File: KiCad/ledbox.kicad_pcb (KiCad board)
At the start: 2 copper layers, 80 x 50 mm, 102 parts, among them CON301 AVR_ISP, J201 Bus, J301 Power B, J302 Port B, J303 Spare, J304 UART, J305 ADC6, J306 ADC7, J401 6.5V-12V, J402 5V, J501 IR LED, J502 Button, Q501 NTR4003N, SW501 Reset, SW502 Push 1, SW503 Push 2, U201 ST485C, U301 ATMEGA88A-AU, U401 AZ1117-5.0, U501 WS2812B, U502 WS2812B, U503 3xWS2812B, Y301 20MHz

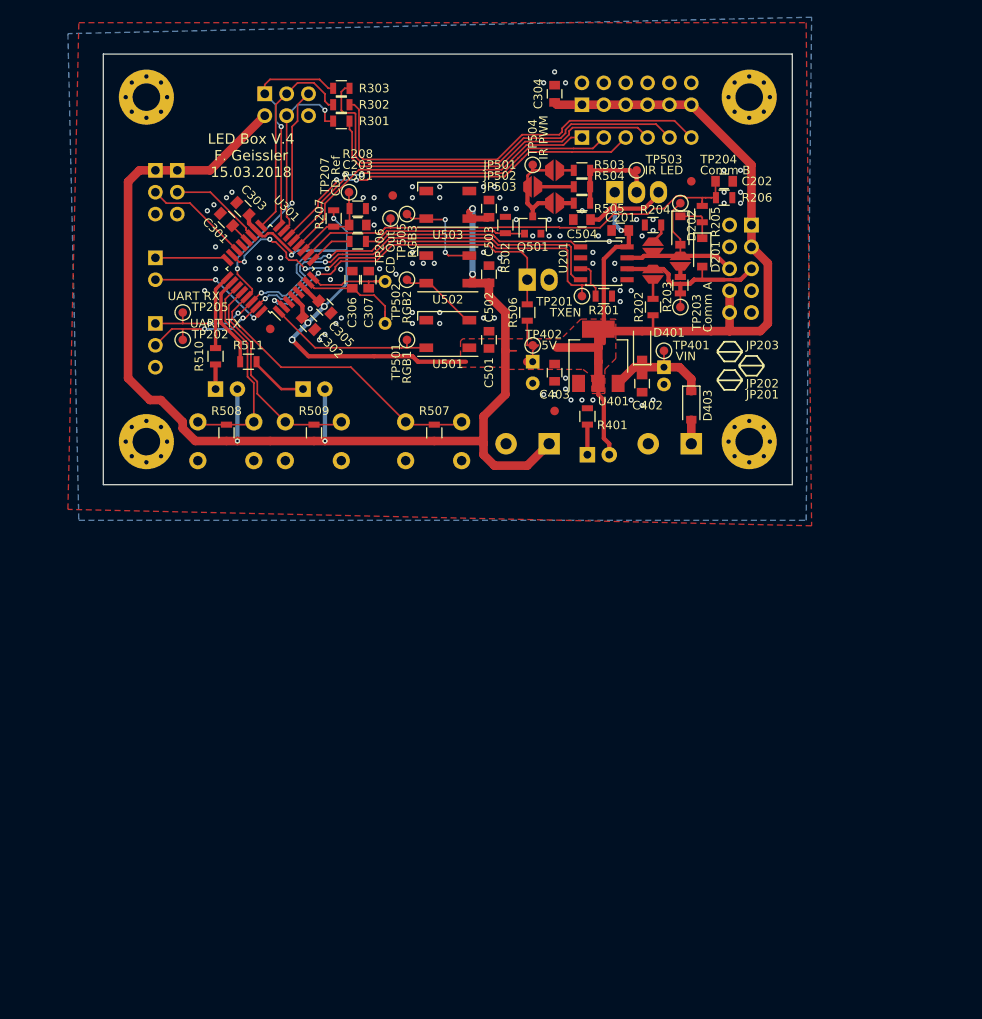
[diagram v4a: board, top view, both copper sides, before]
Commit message: Version 4 Shift Register
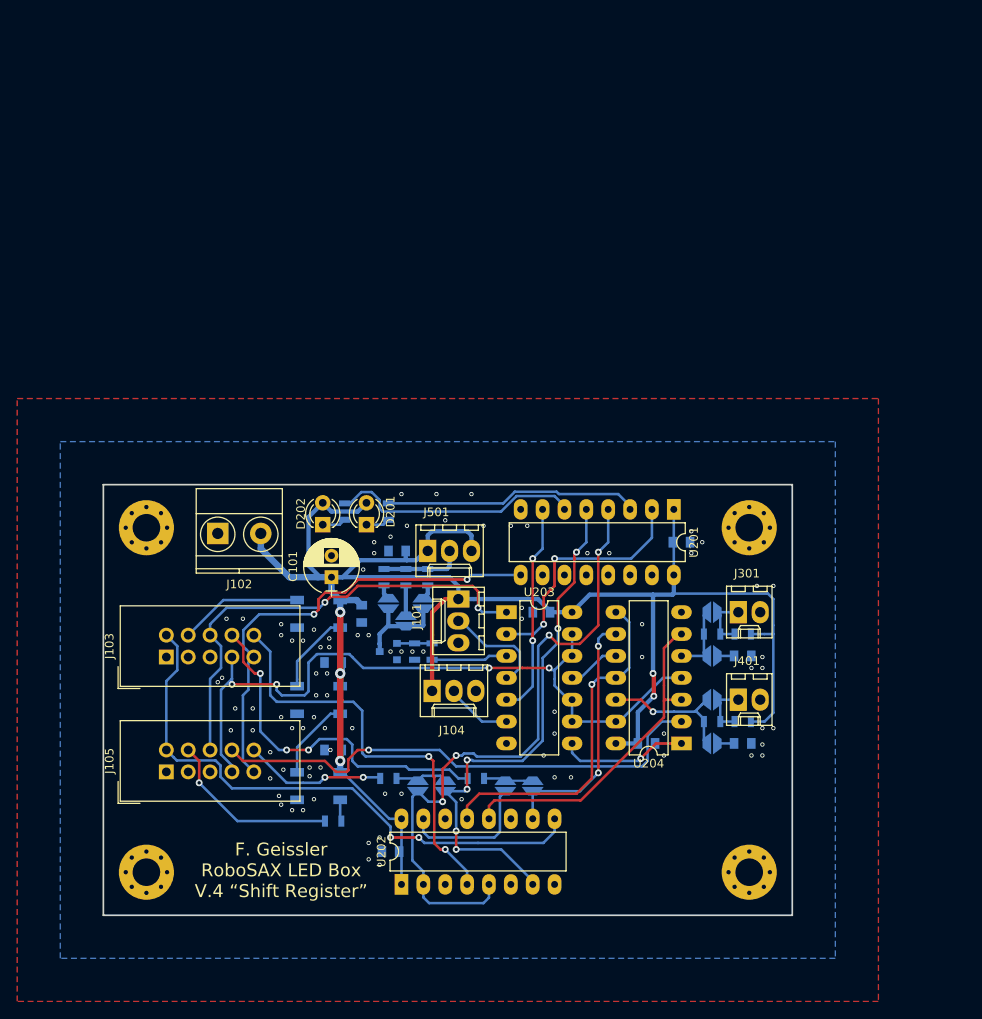
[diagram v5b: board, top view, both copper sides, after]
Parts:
- removed C302, C303, C304, C305, C402, C403: 100n, Capacitors_SMD:C_0805
- removed C306, C307: 22p, Capacitors_SMD:C_0805
- removed C404: 47u, Capacitors_THT:CP_Radial_D6.3mm_P2.50mm
- removed CON301: AVR_ISP, Connectors_IDC:IDC-Header_2x03_Pitch2.54mm_Straight
- removed D401: 1N4148, Diodes_SMD:D_SOD-123
- removed D402, D502: LED2, LEDs:LED_D3.0mm
- removed D403: PMEG4010ER, Diodes_SMD:D_SOD-123
- removed D501: LED1, LEDs:LED_D3.0mm
- removed the G*** at (139.0, 89.0)
- removed the G*** at (140.0, 75.0)
- removed the G*** at (140.0, 56.0)
- removed J201: Bus, Connectors_IDC:IDC-Header_2x05_Pitch2.54mm_Straight
- removed J302: Port B, Socket_Strips:Socket_Strip_Straight_1x06_Pitch2.54mm
- removed J303: Spare, Socket_Strips:Socket_Strip_Straight_1x02_Pitch2.54mm
- removed J304: UART, Socket_Strips:Socket_Strip_Straight_1x03_Pitch2.54mm
- removed J305: ADC6, Socket_Strips:Socket_Strip_Straight_1x03_Pitch2.54mm
- removed J306: ADC7, Socket_Strips:Socket_Strip_Straight_1x03_Pitch2.54mm
- removed J402: 5V, TerminalBlock_MetzConnect:TerminalBlock_MetzConnect_Type055_RT01502HDWU_Pitch5.00mm
- removed J502: Button, Connectors_Molex:Molex_KK-6410-02_02x2.54mm_Straight
- removed R203: 150, Resistors_SMD:R_0805
- removed R204, R303: 1k, Resistors_SMD:R_0805
- removed R205: 100, Resistors_SMD:R_0805
- removed R206: 22k, Resistors_SMD:R_0805
- removed R207: 3k3, Resistors_SMD:R_0805
- removed R208: 2k2, Resistors_SMD:R_0805
- removed R506, R507, R508, R509: 10k, Resistors_SMD:R_0805
- removed R510, R511: 430, Resistors_SMD:R_0805
- removed the REF** at (133.6, 66.4)
- removed the REF** at (168.3, 64.8)
- removed the REF** at (152.4, 91.4)
- removed the REF** at (119.4, 81.9)
- removed the REF** at (105.0, 95.0)
- removed the REF** at (105.0, 55.0)
- removed the REF** at (175.0, 55.0)
- removed the REF** at (175.0, 95.0)
- removed SW501: Reset, Buttons_Switches_THT:SW_PUSH_6mm_h5mm
- removed SW502: Push 1, Buttons_Switches_THT:SW_PUSH_6mm_h5mm
- removed SW503: Push 2, Buttons_Switches_THT:SW_PUSH_6mm_h5mm
- removed TP201: TXEN, Test:TEST_10
- removed TP202: UART TX, Test:TEST_10
- removed TP203: Comm A, Test:TEST_10
- removed TP204: Comm B, Test:TEST_10
- removed TP205: UART RX, Test:TEST_10
- removed TP206: CD Out, Test:TEST_10
- removed TP207: CD Ref, Test:TEST_10
- removed TP401: VIN, Test:TEST_10
- removed TP402: 5V, Test:TEST_10
- removed TP501: RGB1, Test:TEST_10
- removed TP502: RGB2, Test:TEST_10
- removed TP503: IR LED, Test:TEST_10
- removed TP504: IR PWM, Test:TEST_10
- removed TP505: RGB3, Test:TEST_10
- removed U301: ATMEGA88A-AU, Housings_QFP:TQFP-32_7x7mm_Pitch0.8mm
- removed U401: AZ1117-5.0, TO_SOT_Packages_SMD:SOT-223-3_TabPin2
- removed Y301: 20MHz, Crystals:Crystal_HC49-U_Vertical
- added C101: 10u, Capacitors_THT:CP_Radial_D6.3mm_P2.50mm, F.Cu at (126.5, 110.7)
- added C204: 100n, Capacitors_SMD:C_0805, B.Cu at (133.3, 142.6)
- added G***: LOGO, LOGO, F.Cu at (162.1, 141.7)
- added J101: Add Input, Connectors_Molex:Molex_KK-6410-03_03x2.54mm_Straight, F.Cu at (141.2, 113.3)
- added J102: 5V, TerminalBlock_Phoenix:TerminalBlock_Phoenix_MKDS1.5-2pol, F.Cu at (113.3, 105.7)
- added J103: To Master, Connectors_IDC:IDC-Header_2x05_Pitch2.54mm_Straight, F.Cu at (107.3, 120.0)
- added J104: Add Output, Connectors_Molex:Molex_KK-6410-03_03x2.54mm_Straight, F.Cu at (138.2, 124.0)
- added J105: To Slave, Connectors_IDC:IDC-Header_2x05_Pitch2.54mm_Straight, F.Cu at (107.3, 133.3)
- added JP204: Add In, SMD_Jumper:Jumper_SMD_02, B.Cu at (146.7, 135.0)
- added JP301: ~Debounce, SMD_Jumper:Jumper_SMD_02, B.Cu at (170.7, 114.8)
- added JP302: Debounce, SMD_Jumper:Jumper_SMD_02, B.Cu at (170.7, 119.9)
- added JP401: ~Debounce, SMD_Jumper:Jumper_SMD_02, B.Cu at (170.7, 125.0)
- added JP402: Debounce, SMD_Jumper:Jumper_SMD_02, B.Cu at (170.7, 130.0)
- added R101: 120, Resistors_SMD:R_0805, B.Cu at (143.3, 134.1)
- added R102: 120, Resistors_SMD:R_0805, B.Cu at (133.1, 134.1)
- added R103: 120, Resistors_SMD:R_0805, B.Cu at (126.7, 139.1)
- added R402: 47k, Resistors_SMD:R_0805, B.Cu at (170.7, 127.5)
- added REF**: MountingHole_3.2mm_M3_Pad_Via, Mounting_Holes:MountingHole_3.2mm_M3_Pad_Via, F.Cu at (105.0, 105.0)
- added REF**: MountingHole_3.2mm_M3_Pad_Via, Mounting_Holes:MountingHole_3.2mm_M3_Pad_Via, F.Cu at (105.0, 145.0)
- added REF**: MountingHole_3.2mm_M3_Pad_Via, Mounting_Holes:MountingHole_3.2mm_M3_Pad_Via, F.Cu at (175.0, 145.0)
- added REF**: MountingHole_3.2mm_M3_Pad_Via, Mounting_Holes:MountingHole_3.2mm_M3_Pad_Via, F.Cu at (175.0, 105.0)
- added U202: 74LS175, Housings_DIP:DIP-16_W7.62mm_LongPads, F.Cu at (134.6, 146.4)
- added U203: 74LS00, Housings_DIP:DIP-14_W7.62mm_LongPads, F.Cu at (146.8, 114.8)
- added U204: 74LS126, Housings_DIP:DIP-14_W7.62mm_LongPads, F.Cu at (167.1, 130.0)
- C201: value 10u -> 100n; moved to B.Cu
- C202: value 22p -> 100n; moved to B.Cu
- C203: value 470p -> 100n; moved to B.Cu
- C301, C501, C502, C503, C504, JP501, Q501, R202, R501, U501, U502: moved to B.Cu
- C401: value 4u7 -> 100n; footprint Capacitors_THT:CP_Radial_D5.0mm_P2.00mm -> Capacitors_SMD:C_0805
- D201, D202: value 1N4148 -> LED; footprint Diodes_SMD:D_SOD-123 -> LEDs:LED_D3.0mm
- J301: value Power B -> Button; footprint Socket_Strips:Socket_Strip_Straight_2x06_Pitch2.54mm -> Connectors_Molex:Molex_KK-6410-02_02x2.54mm_Straight; moved to F.Cu
- J401: value 6.5V-12V -> Button; footprint TerminalBlock_MetzConnect:TerminalBlock_MetzConnect_Type055_RT01502HDWU_Pitch5.00mm -> Connectors_Molex:Molex_KK-6410-02_02x2.54mm_Straight; moved to F.Cu
- J501: moved to F.Cu
- JP201: value COMMA PU -> Single Out; moved to B.Cu
- JP202: value TERM -> Add Out; moved to B.Cu
- JP203: value COMMB PD -> Single In; moved to B.Cu
- JP502: value IR 24mA -> IR 36mA; moved to B.Cu
- JP503: value IR 48mA -> IR 76mA; moved to B.Cu
- R201: value 10k -> 1k; moved to B.Cu
- R301: value 1k -> 4k7; moved to B.Cu
- R302: value 1k -> 47k; moved to B.Cu
- R401: value 2k2 -> 4k7; moved to B.Cu
- R502: value 100k -> 47k; moved to B.Cu
- R503: value 300 -> 220; moved to B.Cu
- R504: value 150 -> 100; moved to B.Cu
- R505: value 75 -> 47; moved to B.Cu
- U201: value ST485C -> 74LS175; footprint Housings_SOIC:SOIC-8_3.9x4.9mm_Pitch1.27mm -> Housings_DIP:DIP-16_W7.62mm_LongPads
- U503: value 3xWS2812B -> WS2812B; moved to B.Cu
- moved C301 78.5 mm to (174.2, 119.9), turned to 0 degrees
- moved R301 75.6 mm to (174.2, 117.3)
- moved R302 75.0 mm to (170.7, 117.3), turned to 0 degrees
- moved U503 69.1 mm to (125.0, 135.0)
- moved C203 68.9 mm to (163.1, 130.0)
- moved JP202 66.8 mm to (139.7, 135.0)
- moved JP201 65.4 mm to (136.5, 135.0)
- moved JP203 64.1 mm to (149.9, 135.0)
- moved J301 61.7 mm to (173.7, 114.8), turned to 0 degrees
- moved C502 58.1 mm to (126.7, 130.8), turned to 180 degrees
- moved C503 55.7 mm to (126.7, 120.7), turned to 180 degrees
- moved C202 54.3 mm to (150.9, 114.8), turned to 180 degrees
- moved D202 53.8 mm to (125.5, 104.6), turned to 90 degrees
- moved JP501 52.6 mm to (137.2, 113.8), turned to 90 degrees
- moved JP502 52.5 mm to (135.1, 115.8), turned to 90 degrees
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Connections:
- C202 pad 1: /Bus/AIN0 -> +5V
- C203 pad 1: /Bus/AIN1 -> +5V
- C301 pad 1: GND -> Net-(C301-Pad1)
- C301 pad 2: Net-(C301-Pad2) -> GND
- C401 pad 1: +12V -> Net-(C401-Pad1)
- D201 pad 2: /Bus/COMM_A -> +5V
- D202 pad 1: Net-(D201-Pad1) -> Net-(D202-Pad1)
- D202 pad 2: /Bus/COMM_B -> +5V
- J301 pad 1: +5V -> Net-(J301-Pad1)
- J401 pad 1: Net-(D403-Pad2) -> Net-(J401-Pad1)
- JP201 pad 1: Net-(JP201-Pad1) -> /Logic/LED_OUT
- JP201 pad 2: /Bus/COMM_A -> /Logic/LED_DATA_OUT
- JP202 pad 1: Net-(JP202-Pad1) -> /Logic/LED_OUT_ADD
- JP202 pad 2: /Bus/COMM_B -> /Logic/LED_DATA_OUT
- JP203 pad 1: /Bus/COMM_B -> /Logic/BTN_OUT
- JP203 pad 2: Net-(JP203-Pad2) -> /Logic/BTN_DATA_OUT
- R201 pad 1: GND -> /Logic/LED_INDICATOR
- R201 pad 2: /Bus/TX_EN -> Net-(D201-Pad1)
- R202 pad 1: +5V -> /Logic/LED_INDICATOR_ADD
- R202 pad 2: Net-(JP201-Pad1) -> Net-(D202-Pad1)
- R301 pad 1: /Controller/PB3 -> +5V
- R301 pad 2: /Controller/MOSI -> Net-(J301-Pad1)
- R302 pad 1: /Controller/PB5 -> Net-(JP301-Pad2)
- R302 pad 2: /Controller/SCK -> Net-(J301-Pad1)
- R401 pad 1: Net-(D402-Pad1) -> +5V
- R401 pad 2: GND -> Net-(J401-Pad1)
- R501 pad 2: /Controller/LED_IR -> /Logic/IR_LED
- U201 pad 1: /Bus/RX -> +5V
- U201 pad 2: GND -> Net-(TP203-Pad1)
- U201 pad 3: /Bus/TX_EN -> /Logic/LED_INDICATOR
- U201 pad 4: /Bus/TX -> /Logic/LED_OUT
- U201 pad 5: GND -> /Logic/LED_OUT_ADD
- U201 pad 6: /Bus/COMM_A -> /Logic/LED_INDICATOR_ADD
- U201 pad 7: /Bus/COMM_B -> Net-(TP205-Pad1)
- U201 pad 8: +5V -> GND
- U501 pad 4: /Controller/RGB_D -> /RGB_IN
- U503 pad 2: Net-(U503-Pad2) -> /Interface/RGB_OUT
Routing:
- net +5V: track 338.5 -> 216.4 mm, vias 10 -> 5
- net /BTN_LOAD: track 0.00 -> 86.0 mm, vias 0 -> 4
- net /Logic/LED_OUT: track 0.00 -> 76.4 mm, vias 0 -> 4
- net /CLK: track 0.00 -> 67.5 mm, vias 0 -> 2
- net /Logic/LED_OUT_ADD: track 0.00 -> 63.2 mm, vias 0 -> 6
- net /Controller/~RESET: track 63.1 -> 0.00 mm, vias 2 -> 0
- net /Bus/TX: track 61.9 -> 0.00 mm, vias 4 -> 0
- net /BTN_DATA_IN: track 0.00 -> 59.7 mm, vias 0 -> 1
- net /Bus/RX: track 57.8 -> 0.00 mm, vias 4 -> 0
- net /Bus/TX_EN: track 57.4 -> 0.00 mm, vias 4 -> 0
- net /Bus/AIN0: track 54.8 -> 0.00 mm
- net /IR_CLK: track 0.00 -> 54.3 mm, vias 0 -> 2
- net /LED_LOAD: track 0.00 -> 53.6 mm, vias 0 -> 2
- net /Controller/PB4: track 49.5 -> 0.00 mm
- net /LED_DATA_IN: track 0.00 -> 49.0 mm, vias 0 -> 2
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- removed copper zone on F.Cu, net +5V
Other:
- net class Default: trace_width 0.2 -> 0.25; via_dia 0.6 -> 0.8; via_drill 0.3 -> 0.4
- board text added: "F. Geissler RoboSAX LED Box V.4 “Shift Register”"
- board text removed: "+"
- board text removed: "-"
- board text removed: "5V"
- board text removed: "LED Box V.4 F. Geissler 15.03.2018"

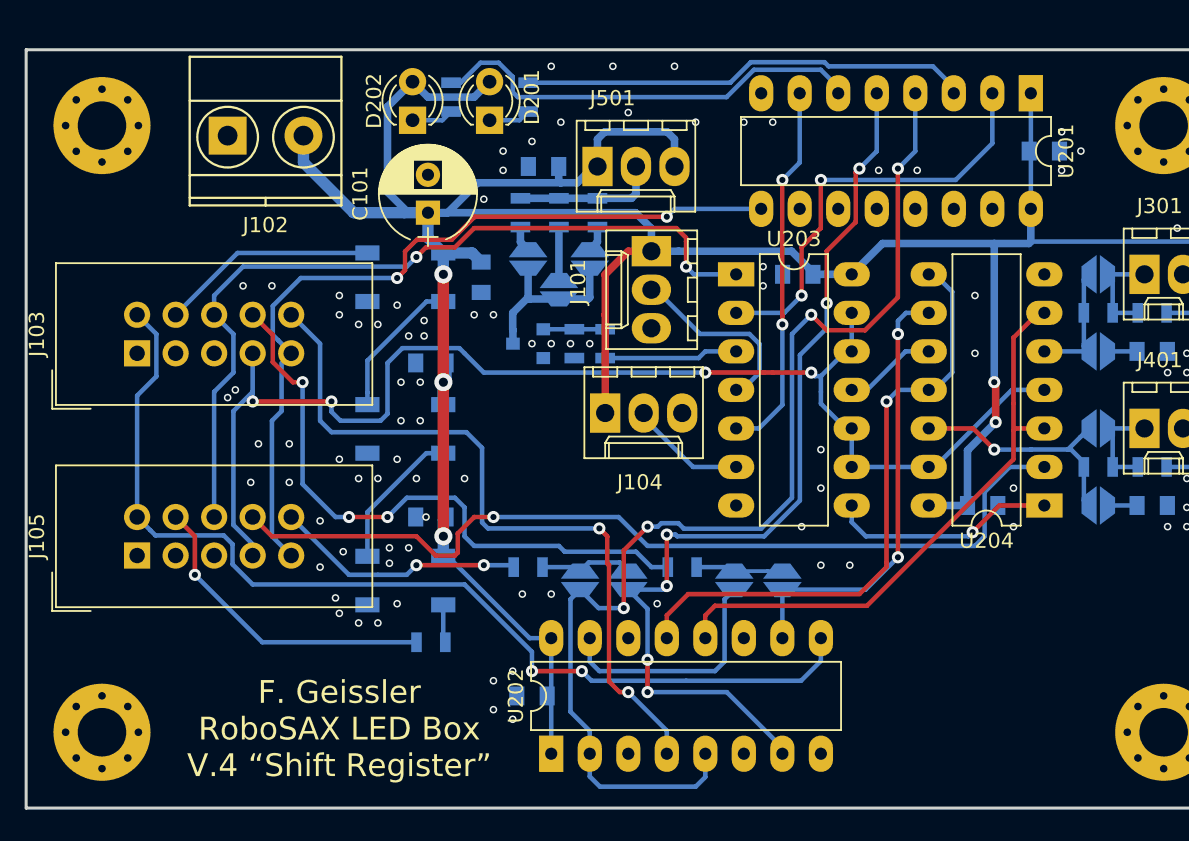
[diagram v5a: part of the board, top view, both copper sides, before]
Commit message: Applied changes for final design, placed test points.
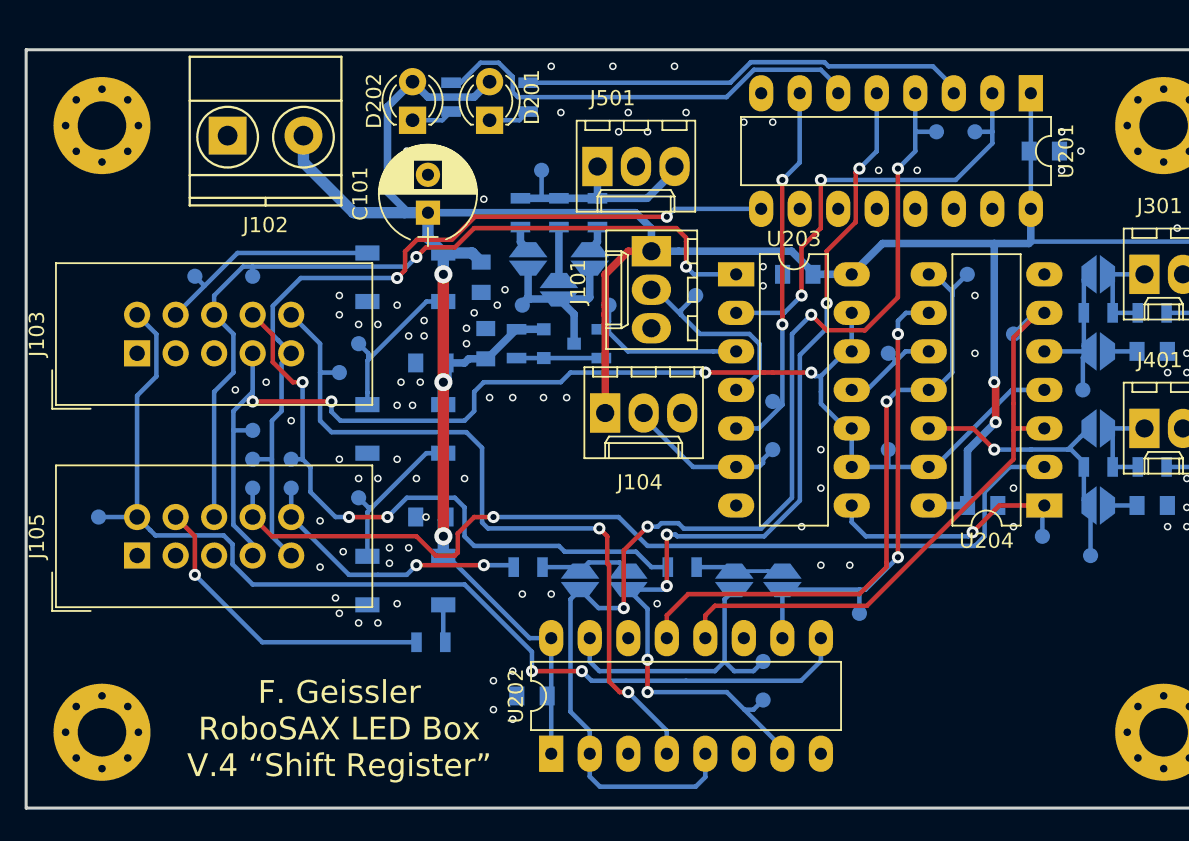
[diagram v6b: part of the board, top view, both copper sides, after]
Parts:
- added TP101: Test_Point, TestPoint:TestPoint_Pad_D1.0mm, B.Cu at (104.8, 130.8)
- added TP102: Test_Point, TestPoint:TestPoint_Pad_D1.0mm, B.Cu at (114.9, 127.0)
- added TP103: Test_Point, TestPoint:TestPoint_Pad_D1.0mm, B.Cu at (114.9, 128.9)
- added TP104: Test_Point, TestPoint:TestPoint_Pad_D1.0mm, B.Cu at (117.5, 127.0)
- added TP105: Test_Point, TestPoint:TestPoint_Pad_D1.0mm, B.Cu at (117.5, 128.9)
- added TP201: LED IN, TestPoint:TestPoint_Pad_D1.0mm, B.Cu at (120.7, 121.3)
- added TP202: Test_Point, TestPoint:TestPoint_Pad_D1.0mm, B.Cu at (114.9, 114.9)
- added TP203: Test_Point, TestPoint:TestPoint_Pad_D1.0mm, B.Cu at (162.6, 105.4)
- added TP204: Test_Point, TestPoint:TestPoint_Pad_D1.0mm, B.Cu at (144.1, 116.2)
- added TP205: Test_Point, TestPoint:TestPoint_Pad_D1.0mm, B.Cu at (149.2, 123.2)
- added TP206: Test_Point, TestPoint:TestPoint_Pad_D1.0mm, B.Cu at (138.4, 116.8)
- added TP207: Test_Point, TestPoint:TestPoint_Pad_D1.0mm, B.Cu at (149.2, 126.4)
- added TP208: LED OUT, TestPoint:TestPoint_Pad_D1.0mm, B.Cu at (160.0, 105.4)
- added TP209: ADD BTN, TestPoint:TestPoint_Pad_D1.0mm, B.Cu at (148.6, 140.3)
- added TP210: ADD OUT, TestPoint:TestPoint_Pad_D1.0mm, B.Cu at (148.6, 142.9)
- added TP211: BTN OUT, TestPoint:TestPoint_Pad_D1.0mm, B.Cu at (154.9, 137.2)
- added TP301: BTN ANA, TestPoint:TestPoint_Pad_D1.0mm, B.Cu at (169.7, 122.4)
- added TP302: BTN LOAD, TestPoint:TestPoint_Pad_D1.0mm, B.Cu at (114.9, 125.1)
- added TP303: ~BTN LOAD, TestPoint:TestPoint_Pad_D1.0mm, B.Cu at (167.0, 132.1)
- added TP304: BTN IN, TestPoint:TestPoint_Pad_D1.0mm, B.Cu at (165.1, 118.7)
- added TP401: BTN ANA, TestPoint:TestPoint_Pad_D1.0mm, B.Cu at (170.2, 133.3)
- added TP402: BTN LOAD, TestPoint:TestPoint_Pad_D1.0mm, B.Cu at (156.8, 126.4)
- added TP403: ~BTN LOAD, TestPoint:TestPoint_Pad_D1.0mm, B.Cu at (156.8, 120.0)
- added TP404: BTN IN, TestPoint:TestPoint_Pad_D1.0mm, B.Cu at (162.1, 114.8)
- added TP501: RGB1, TestPoint:TestPoint_Pad_D1.0mm, B.Cu at (111.1, 114.9)
- added TP502: RGB2, TestPoint:TestPoint_Pad_D1.0mm, B.Cu at (121.9, 119.4)
- added TP503: IR LED, TestPoint:TestPoint_Pad_D1.0mm, B.Cu at (134.0, 108.0)
- added TP504: IR PWM, TestPoint:TestPoint_Pad_D1.0mm, B.Cu at (132.7, 116.8)
- added TP505: RGB3, TestPoint:TestPoint_Pad_D1.0mm, B.Cu at (121.9, 129.5)
- Q501: value NTR4003N -> Q_PMOS_GSD; footprint TO_SOT_Packages_SMD:SOT-23 -> Package_TO_SOT_SMD:SOT-23
- moved C504 12.3 mm to (130.3, 119.4), turned to 90 degrees
- moved R502 3.81 mm to (132.3, 119.4)
- moved Q501 2.03 mm to (135.1, 119.4), turned to 0 degrees
- moved R501 0.25 mm to (137.9, 119.4), turned to 90 degrees
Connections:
- J501 pad 1: +5V -> /Interface/IR_LED_DRV
- J501 pad 2: /Interface/IR_LED_DRV -> GND
- J501 pad 3: +5V -> /Interface/IR_LED_DRV
- Q501 pad 2: GND -> +5V
- R502 pad 1: GND -> Net-(Q501-Pad1)
- R502 pad 2: Net-(Q501-Pad1) -> +5V
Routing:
- net +5V: track 216.4 -> 201.1 mm
- net /Interface/IR_LED_DRV: track 9.72 -> 15.3 mm
- net Net-(JP401-Pad2): track 16.1 -> 19.5 mm
- net Net-(JP204-Pad1): track 16.0 -> 19.0 mm
- net /Logic/ADD_OUT: track 7.74 -> 10.8 mm
- net Net-(JP301-Pad2): track 8.31 -> 11.0 mm
- net /Logic/button_mux/BTN_OUT: track 39.3 -> 41.9 mm
- net /CLK: track 67.5 -> 70.0 mm
- net /Logic/IR_LED: track 8.82 -> 11.3 mm
- net Net-(TP303-Pad1): track 15.0 -> 17.1 mm
- net /LED_DATA_OUT: track 16.6 -> 18.5 mm
- net /BTN_DATA_IN: track 59.7 -> 61.6 mm
- net /Logic/button_mux_add/BTN_OUT: track 40.7 -> 42.5 mm
- net /Logic/ADD_IN: track 12.5 -> 14.2 mm
- net /Logic/BTN_OUT: track 29.5 -> 31.1 mm
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
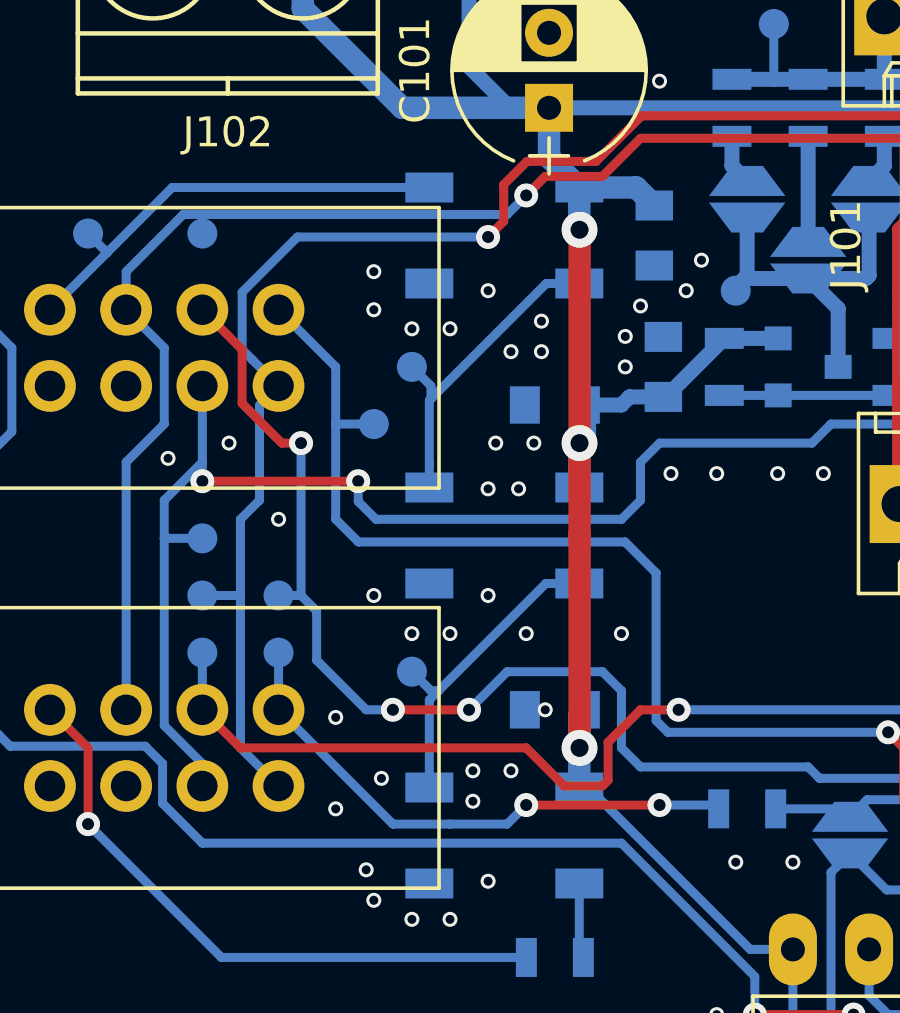
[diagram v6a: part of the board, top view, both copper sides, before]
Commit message: paralleled RGB leds
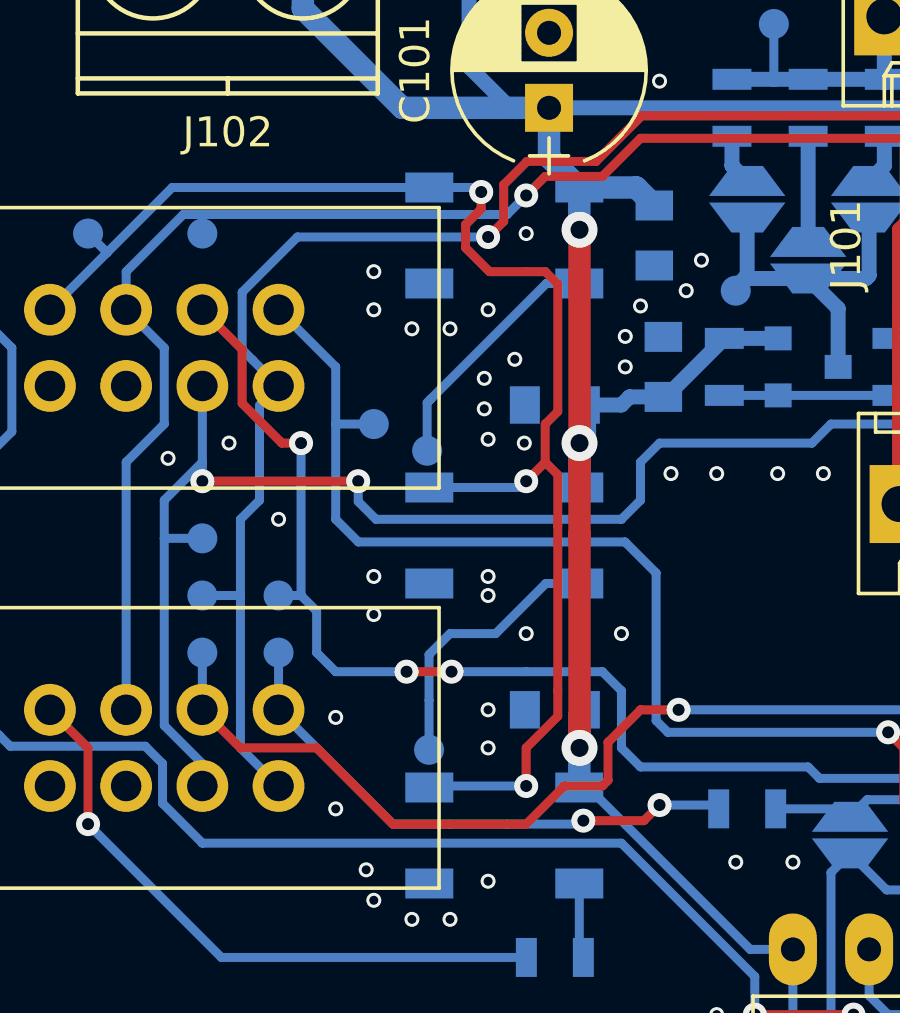
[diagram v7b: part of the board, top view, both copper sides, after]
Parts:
- Q501: value Q_PMOS_GSD -> AO3415A
- moved TP502 2.84 mm to (122.4, 122.2)
- moved TP505 2.67 mm to (122.5, 132.1)
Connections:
- U502 pad 4: Net-(TP502-Pad1) -> /RGB_IN
- U503 pad 4: Net-(TP505-Pad1) -> /RGB_IN
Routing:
- net /RGB_IN: track 15.2 -> 47.6 mm, vias 0 -> 3
- net Net-(TP502-Pad1): track 10.8 -> 8.40 mm
- net Net-(TP505-Pad1): track 10.7 -> 9.16 mm
- net /BTN_DATA_OUT: track 42.2 -> 41.0 mm
- net /BTN_DATA_IN: track 61.6 -> 62.7 mm
- net GND: vias 90 -> 86
